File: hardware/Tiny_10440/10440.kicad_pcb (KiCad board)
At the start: 2 copper layers, 87.5 x 16 mm, 49 parts, among them J2 Battery, J3 GPIO, J4 USB_B_Micro, J5 LEDs, J7 GPIO/Power, Q1 BSS806N, Q2 BSS806N, Q3 BSS806N, Q4 BSS806N, SW1 Mode, SW2 Power, U1 STM32L072KZUx, U2 AP2210N-3.3TRG1, U3 MCP73831T-2ACI_OT, U4 ESD7002WTT1G

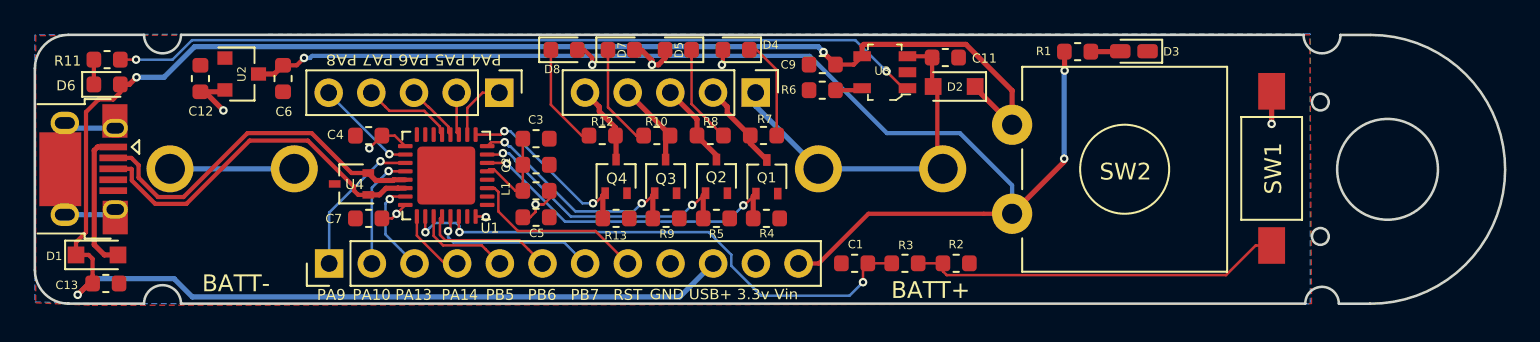
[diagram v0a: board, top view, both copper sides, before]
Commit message: Use STM32F412CGUx (Regular & Tiny)
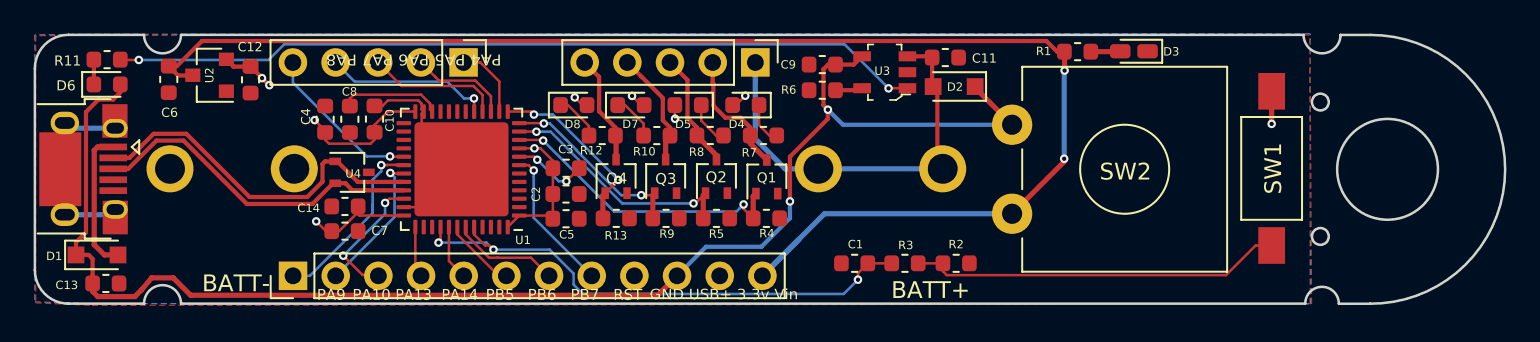
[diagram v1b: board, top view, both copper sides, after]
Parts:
- removed L1: Bead, Inductor_SMD:L_0603_1608Metric
- added C10: 100nf, Capacitor_SMD:C_0603_1608Metric, F.Cu at (78.3, 97.0)
- added C14: 100nf, Capacitor_SMD:C_0603_1608Metric, F.Cu at (76.6, 102.2)
- added C8: 4.7uF, Capacitor_SMD:C_0603_1608Metric, F.Cu at (76.8, 97.0)
- C3: value 10nf -> 100nf
- U1: value STM32L072KZUx -> STM32F412CGUx; footprint Package_DFN_QFN:QFN-32-1EP_5x5mm_P0.5mm_EP3.45x3.45mm -> Package_DFN_QFN:QFN-48-1EP_7x7mm_P0.5mm_EP5.6x5.6mm
- moved C6 6.81 mm to (66.1, 94.7)
- moved D4 3.34 mm to (100.4, 96.2)
- moved D5 3.34 mm to (97.0, 96.2)
- moved D7 3.34 mm to (93.6, 96.2)
- moved D8 3.34 mm to (90.2, 96.2)
- moved C12 2.99 mm to (70.9, 94.7), turned to 270 degrees
- moved J3 2.79 mm to (83.6, 93.6)
- moved C4 2.77 mm to (75.4, 97.0), turned to 90 degrees
- moved C3 2.51 mm to (89.7, 99.9)
- moved C2 2.49 mm to (89.7, 101.5)
- moved J7 2.27 mm to (73.5, 106.3)
- moved U2 1.92 mm to (68.5, 94.4), turned to 180 degrees
- moved J5 1.79 mm to (101.0, 93.6)
- moved C5 1.79 mm to (89.7, 102.9)
- moved C7 1.60 mm to (76.6, 103.7), turned to 0 degrees
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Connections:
- C2 pad 1: Net-(C2-Pad1) -> +3V3
- C3 pad 1: Net-(C2-Pad1) -> +3V3
- U1 pad 1: (no net) -> +3V3
- U1 pad 10: /PA4 -> /PWM1
- U1 pad 11: /PA5 -> /PWM2
- U1 pad 12: /PA6 -> /PWM3
- U1 pad 13: /PA7 -> /PWM4
- U1 pad 14: (no net) -> /PA4
- U1 pad 15: (no net) -> /PA5
- U1 pad 16: GND -> /PA6
- U1 pad 17: +3V3 -> /PA7
- U1 pad 18: /PA8 -> (no net)
- U1 pad 19: /PA9 -> (no net)
- U1 pad 20: /PA10 -> (no net)
- U1 pad 21: /USB_D- -> (no net)
- U1 pad 22: /USB_D+ -> Net-(C8-Pad1)
- U1 pad 23: /PA13 -> GND
- U1 pad 25: /PA14 -> (no net)
- U1 pad 26: /BUTTON -> (no net)
- U1 pad 27: /PB5 -> (no net)
- U1 pad 28: /PB6 -> (no net)
- U1 pad 29: /PB7 -> /PA8
- U1 pad 3: /RESET -> (no net)
- U1 pad 30: /BUTTON -> /PA9
- U1 pad 31: GND -> /PA10
- U1 pad 32: +3V3 -> /USB_D-
- U1 pad 33: GND -> /USB_D+
- U1 pad 4: GND -> (no net)
- U1 pad 5: Net-(C2-Pad1) -> (no net)
- U1 pad 6: /PWM1 -> (no net)
- U1 pad 7: /PWM2 -> /RESET
- U1 pad 8: /PWM3 -> GND
- U1 pad 9: /PWM4 -> +3V3
- U4 pad 1: /USB_D+ -> /USB_D-
- U4 pad 2: /USB_D- -> /USB_D+
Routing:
- net /VUSB: track 116.7 -> 86.3 mm, vias 3 -> 2
- net +3V3: track 18.5 -> 32.6 mm, vias 9 -> 10
- net /VIN: track 75.1 -> 86.3 mm, vias 3 -> 2
- net GND: track 13.7 -> 23.1 mm, vias 0 -> 2
- net Net-(C8-Pad1): track 0.00 -> 6.06 mm
- net Net-(C2-Pad1): track 5.81 -> 0.00 mm
- net /PA6: track 3.41 -> 8.00 mm
- net /PA7: track 5.45 -> 9.91 mm, vias 0 -> 1
- net /PB7: track 10.1 -> 6.42 mm, vias 1 -> 0
- net /PB6: track 7.96 -> 4.38 mm
- net Net-(D4-Pad1): track 6.03 -> 2.50 mm
- net /PA8: track 6.11 -> 9.63 mm
- net Net-(D8-Pad1): track 6.28 -> 2.77 mm
- net Net-(D7-Pad1): track 6.21 -> 2.71 mm
- net /PA5: track 2.55 -> 5.92 mm
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
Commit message: Finish updating Small board with STM32F4
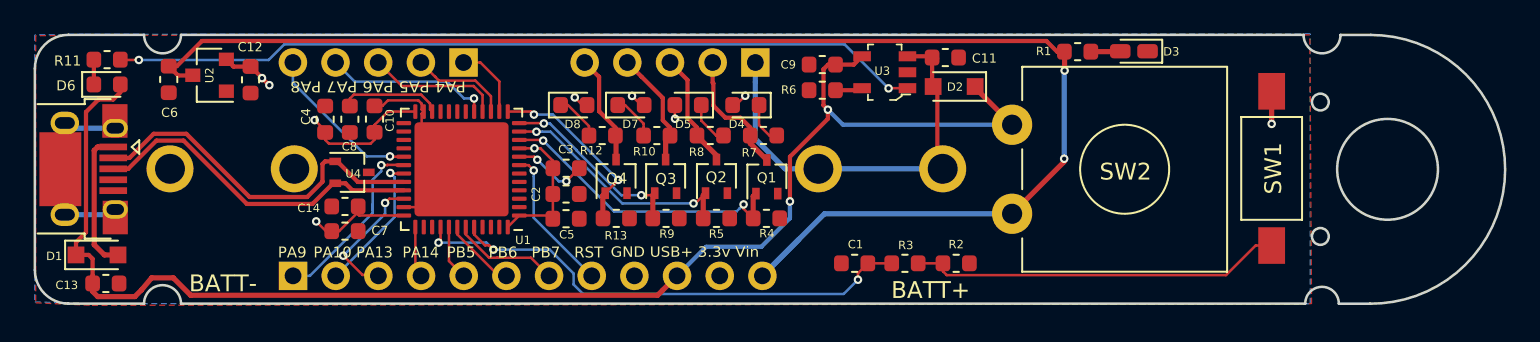
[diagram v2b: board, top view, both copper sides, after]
